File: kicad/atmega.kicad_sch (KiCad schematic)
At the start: 31 parts, among them J1 Conn_01x04_Pin, J3 Conn_02x03_Odd_Even, J4 Conn_01x03_Pin, J5 Conn_01x06_Pin, J6 Conn_01x04_Pin, SW1 SW_Push, U1 ATmega164P-20P, Y1 18.341MHz

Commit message: minor schematic updayes
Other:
- note added: "Note: can use internal PAx pull-ups (possibly) Maybe change to 680R to use similar resistors to the LEDs"
- note removed: "Note: can use internal PAx pull-ups (possibly)"
- moved on the sheet: R18, R9
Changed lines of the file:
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@@
 		)
 	)
-	(text "Note: can use internal PAx pull-ups (possibly)\n"
+	(text "Note: can use internal PAx pull-ups (possibly)\nMaybe change to 680R to use similar resistors to the LEDs"
 		(exclude_from_sim no)
-		(at 179.832 18.796 0)
+		(at 155.956 29.718 0)
 		(effects
 			(font
 				(size 1.27 1.27)
 			)
+			(justify left)
 		)
 	)
@@
 	(wire
 		(pts
-			(xy 189.23 81.28) (xy 189.23 77.47)
+			(xy 207.01 72.39) (xy 207.01 68.58)
 		)
 		(stroke
@@
 	(wire
 		(pts
-			(xy 193.04 81.28) (xy 189.23 81.28)
+			(xy 210.82 72.39) (xy 207.01 72.39)
 		)
 		(stroke
@@
 	(wire
 		(pts
-			(xy 193.04 85.09) (xy 180.34 85.09)
+			(xy 210.82 76.2) (xy 198.12 76.2)
 		)
 		(stroke
@@
 	(wire
 		(pts
-			(xy 180.34 85.09) (xy 180.34 77.47)
+			(xy 198.12 76.2) (xy 198.12 68.58)
 		)
 		(stroke
@@
 	(hierarchical_label "SCL"
 		(shape bidirectional)
-		(at 193.04 81.28 0)
+		(at 210.82 72.39 0)
 		(effects
 			(font
@@
 	(hierarchical_label "SDA"
 		(shape bidirectional)
-		(at 193.04 85.09 0)
+		(at 210.82 76.2 0)
 		(effects
 			(font
@@
 	(symbol
 		(lib_id "Device:R")
-		(at 189.23 73.66 0)
+		(at 207.01 64.77 0)
 		(unit 1)
 		(exclude_from_sim no)
@@
 		(fields_autoplaced yes)
 		(property "Reference" "R18"
-			(at 191.77 72.3899 0)
+			(at 209.55 63.4999 0)
 			(effects
 				(font
@@
 		)
 		(property "Value" "4K7"
-			(at 191.77 74.9299 0)
+			(at 209.55 66.0399 0)
 			(effects
 				(font
@@
 		)
 		(property "Footprint" "Resistor_THT:R_Axial_DIN0207_L6.3mm_D2.5mm_P10.16mm_Horizontal"
-			(at 187.452 73.66 90)
+			(at 205.232 64.77 90)
 			(effects
 				(font
@@
 		)
 		(property "Datasheet" "~"
-			(at 189.23 73.66 0)
+			(at 207.01 64.77 0)
 			(effects
 				(font
@@
 		)
 		(property "Description" "Resistor"
-			(at 189.23 73.66 0)
+			(at 207.01 64.77 0)
 			(effects
 				(font
@@
 	(symbol
 		(lib_id "power:VCC")
-		(at 189.23 69.85 0)
+		(at 207.01 60.96 0)
 		(unit 1)
 		(exclude_from_sim no)
@@
 		(fields_autoplaced yes)
 		(property "Reference" "#PWR040"
-			(at 189.23 73.66 0)
+			(at 207.01 64.77 0)
 			(effects
 				(font
@@
 		)
 		(property "Value" "VCC"
-			(at 189.23 64.77 0)
+			(at 207.01 55.88 0)
 			(effects
 				(font
@@
 		)
 		(property "Footprint" ""
-			(at 189.23 69.85 0)
+			(at 207.01 60.96 0)
 			(effects
 				(font
@@
 		)
 		(property "Datasheet" ""
-			(at 189.23 69.85 0)
+			(at 207.01 60.96 0)
 			(effects
 				(font
@@
 		)
 		(property "Description" "Power symbol creates a global label with name \"VCC\""
-			(at 189.23 69.85 0)
+			(at 207.01 60.96 0)
 			(effects
 				(font
@@
 	(symbol
 		(lib_id "power:VCC")
-		(at 180.34 69.85 0)
+		(at 198.12 60.96 0)
 		(unit 1)
 		(exclude_from_sim no)
@@
 		(fields_autoplaced yes)
 		(property "Reference" "#PWR041"
-			(at 180.34 73.66 0)
+			(at 198.12 64.77 0)
 			(effects
 				(font
@@
 		)
 		(property "Value" "VCC"
-			(at 180.34 64.77 0)
+			(at 198.12 55.88 0)
 			(effects
 				(font
@@
 		)
 		(property "Footprint" ""
-			(at 180.34 69.85 0)
+			(at 198.12 60.96 0)
 			(effects
 				(font
@@
 		)
 		(property "Datasheet" ""
-			(at 180.34 69.85 0)
+			(at 198.12 60.96 0)
 			(effects
 				(font
@@
 		)
 		(property "Description" "Power symbol creates a global label with name \"VCC\""
-			(at 180.34 69.85 0)
+			(at 198.12 60.96 0)
 			(effects
 				(font
@@
 	(symbol
 		(lib_id "Device:R")
-		(at 180.34 73.66 0)
+		(at 198.12 64.77 0)
 		(unit 1)
 		(exclude_from_sim no)
@@
 		(fields_autoplaced yes)
 		(property "Reference" "R9"
-			(at 182.88 72.3899 0)
+			(at 200.66 63.4999 0)
 			(effects
 				(font
@@
 		)
 		(property "Value" "4K7"
-			(at 182.88 74.9299 0)
+			(at 200.66 66.0399 0)
 			(effects
 				(font
@@
 		)
 		(property "Footprint" "Resistor_THT:R_Axial_DIN0207_L6.3mm_D2.5mm_P10.16mm_Horizontal"
-			(at 178.562 73.66 90)
+			(at 196.342 64.77 90)
 			(effects
 				(font
@@
 		)
 		(property "Datasheet" "~"
-			(at 180.34 73.66 0)
+			(at 198.12 64.77 0)
 			(effects
 				(font
@@
 		)
 		(property "Description" "Resistor"
-			(at 180.34 73.66 0)
+			(at 198.12 64.77 0)
 			(effects
 				(font

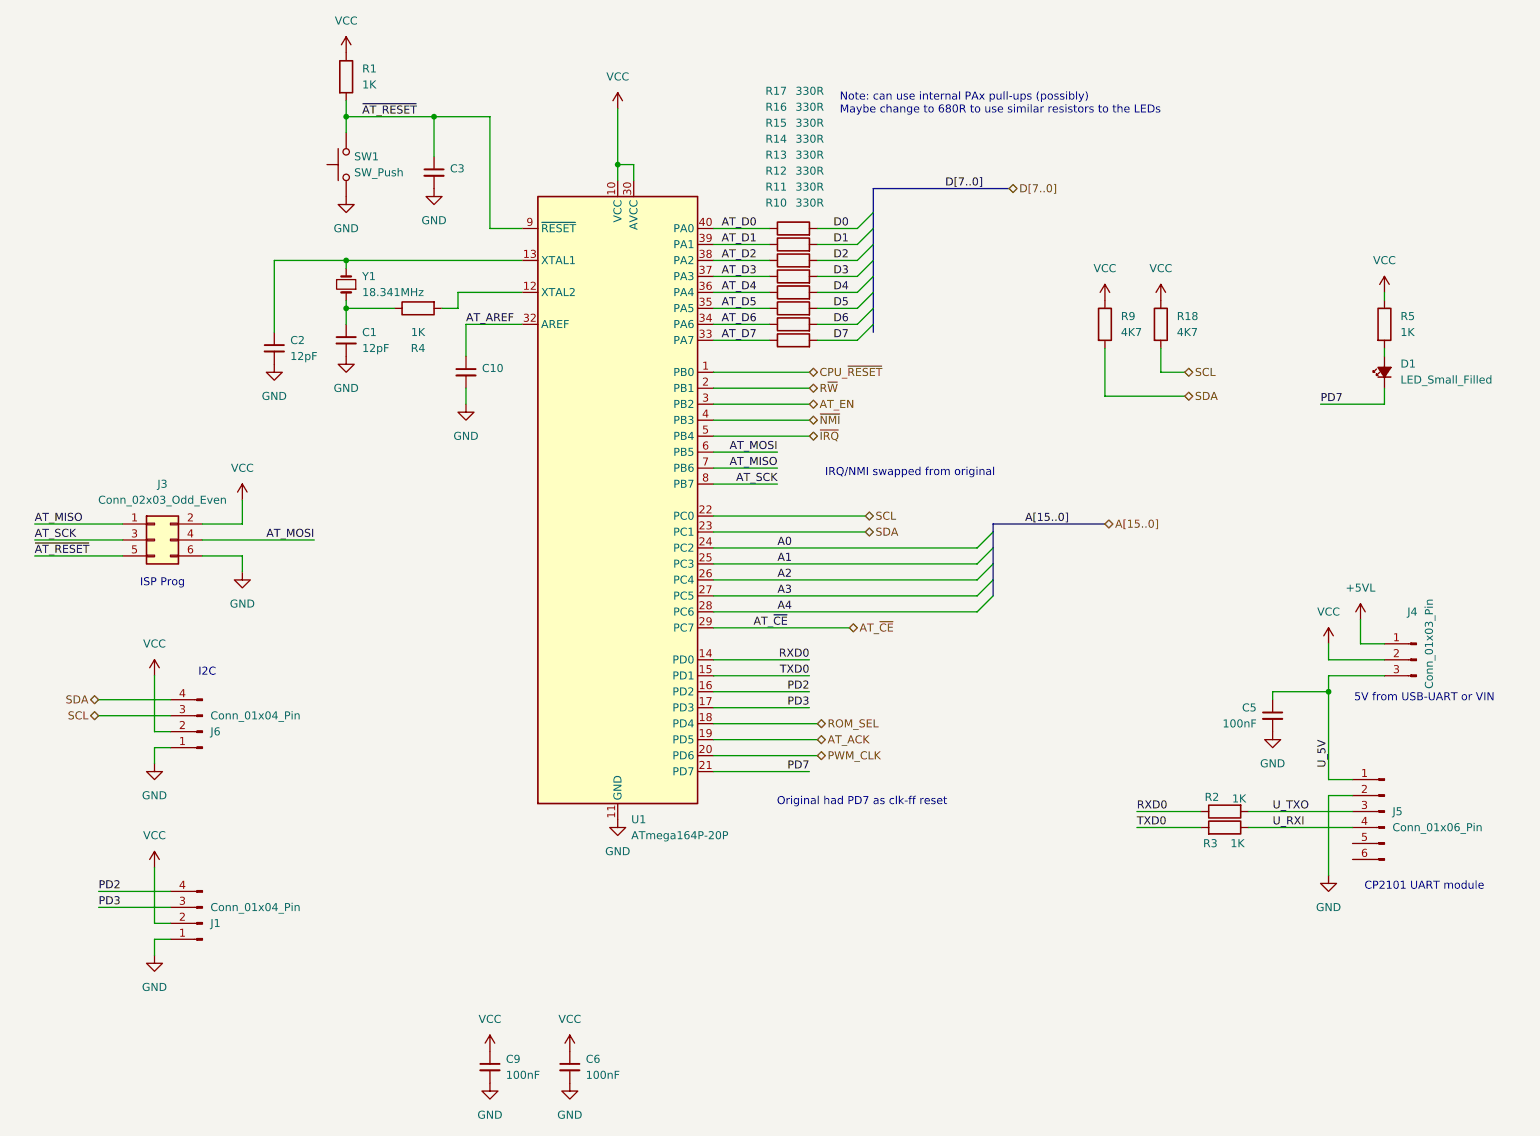
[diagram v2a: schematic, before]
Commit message: value updates, fix ROM ~WE
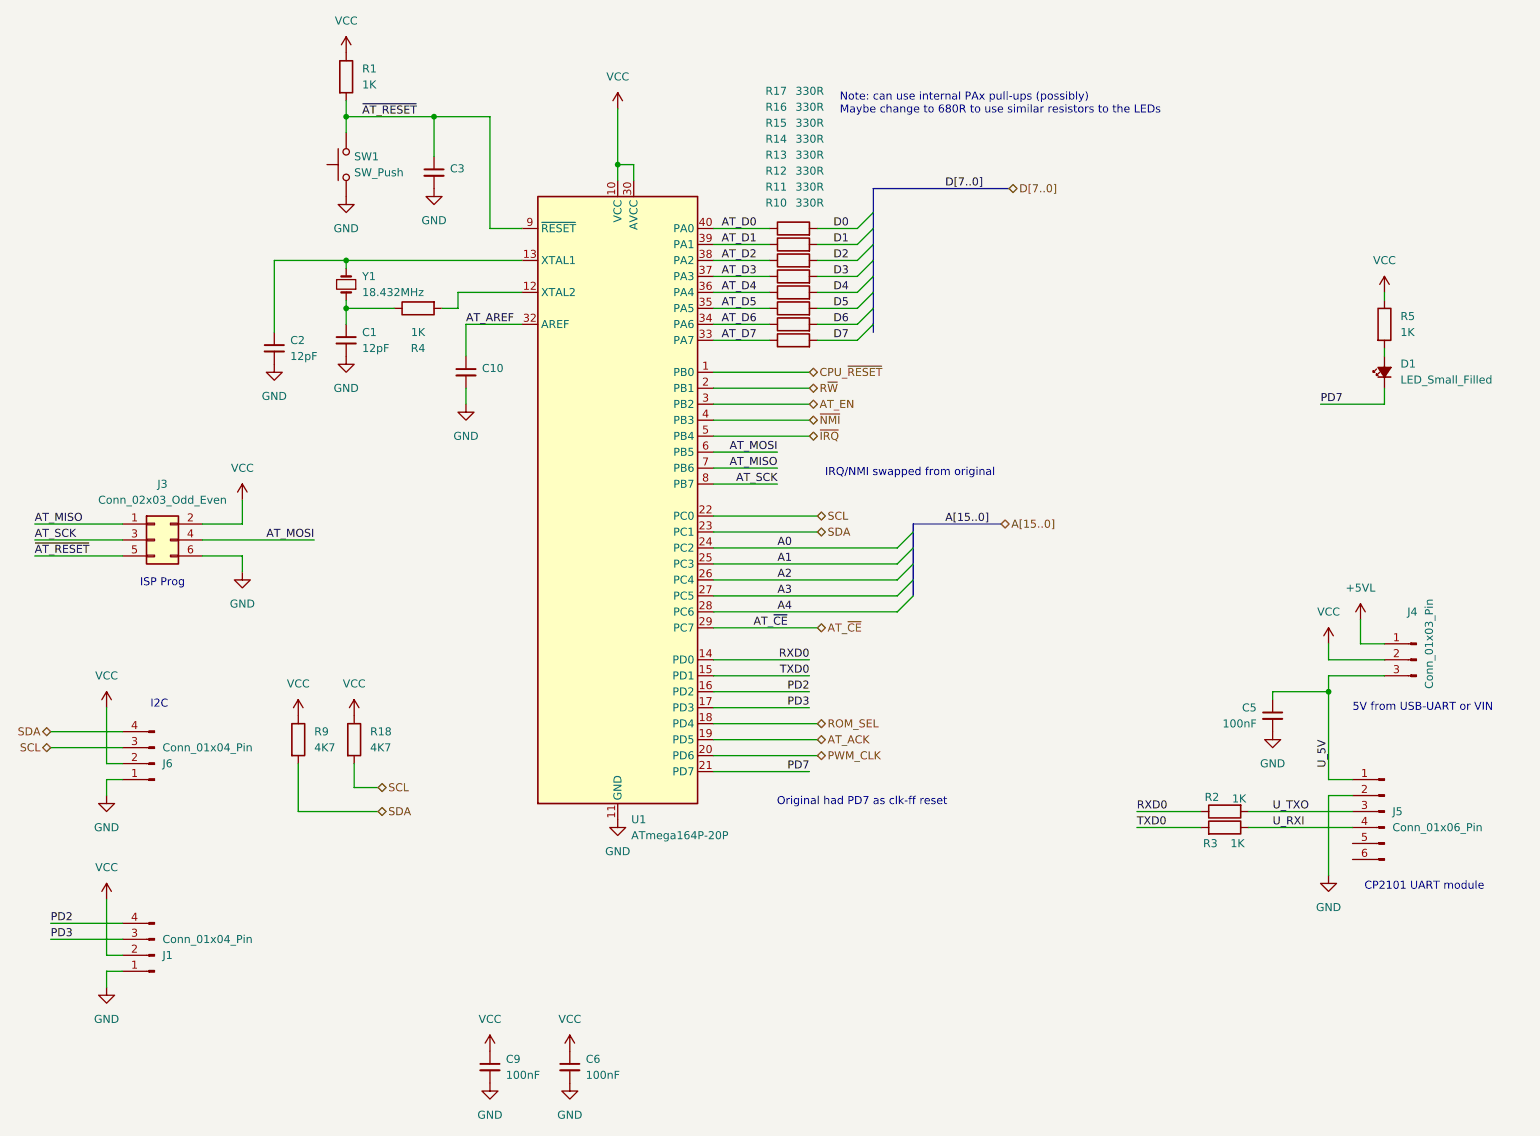
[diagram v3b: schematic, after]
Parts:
- Y1: value 18.341MHz -> 18.432MHz
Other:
- moved on the sheet: J1, J6, R18, R9

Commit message: pcb updates, remove resistor on xtal, smaller board
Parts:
- removed R4: 1K, Resistor_THT:R_Axial_DIN0207_L6.3mm_D2.5mm_P10.16mm_Horizontal, symbol Device:R
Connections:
- net AT_XTO: now reaches C1.1, Y1.1
- net AT_XTO: now also U1.12 (XTAL2)
- net AT_XTI: now reaches C2.1, U1.13 (XTAL1), Y1.2
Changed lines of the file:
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@@
 	(wire
 		(pts
-			(xy 92.71 62.23) (xy 95.25 62.23)
-		)
-		(stroke
-			(width 0)
-			(type default)
-		)
-	)
-	(wire
-		(pts
 			(xy 135.89 87.63) (xy 146.05 87.63)
 		)
@@
 	(wire
 		(pts
-			(xy 77.47 62.23) (xy 85.09 62.23)
+			(xy 77.47 62.23) (xy 95.25 62.23)
 		)
 		(stroke
@@
 		)
 	)
+	(label "AT_XTI"
+		(at 96.52 54.61 0)
+		(effects
+			(font
+				(size 1.27 1.27)
+			)
+			(justify left bottom)
+		)
+	)
 	(label "D4"
 		(at 154.94 59.69 0)
@@
 		)
 	)
+	(label "AT_XTO"
+		(at 96.52 59.69 0)
+		(effects
+			(font
+				(size 1.27 1.27)
+			)
+			(justify left bottom)
+		)
+	)
 	(label "AT_MISO"
 		(at 27.94 96.52 0)
@@
 					(unit 1)
 				)
-			)
-		)
-	)
-	(symbol
-		(lib_id "Device:R")
-		(at 88.9 62.23 90)
-		(mirror x)
-		(unit 1)
-		(exclude_from_sim no)
-		(in_bom yes)
-		(on_board yes)
-		(dnp no)
-		(property "Reference" "R4"
-			(at 88.9 68.58 90)
-			(effects
-				(font
-					(size 1.27 1.27)
-				)
-			)
-		)
-		(property "Value" "1K"
-			(at 88.9 66.04 90)
-			(effects
-				(font
-					(size 1.27 1.27)
-				)
-			)
-		)
-		(property "Footprint" "Resistor_THT:R_Axial_DIN0207_L6.3mm_D2.5mm_P10.16mm_Horizontal"
-			(at 88.9 60.452 90)
-			(effects
-				(font
-					(size 1.27 1.27)
-				)
-				(hide yes)
-			)
-		)
-		(property "Datasheet" "~"
-			(at 88.9 62.23 0)
-			(effects
-				(font
-					(size 1.27 1.27)
-				)
-				(hide yes)
-			)
-		)
-		(property "Description" "Resistor"
-			(at 88.9 62.23 0)
-			(effects
-				(font
-					(size 1.27 1.27)
-				)
-				(hide yes)
-			)
-		)
-		(pin "2"
-		)
-		(pin "1"
-		)
-		(instances
-			(project "6502atty"
-				(path "/f612fa92-d5fa-4cb5-a666-c1c24e7cbb30/83b01514-6b56-4f3e-9a42-17260f217a5e"
-					(reference "R4")
-					(unit 1)
-				)

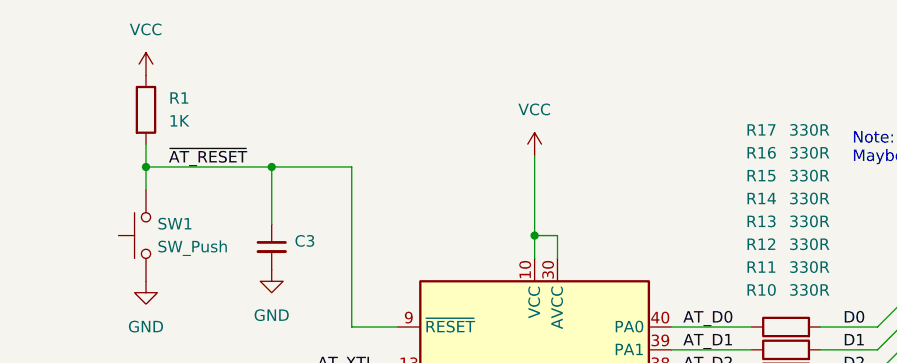
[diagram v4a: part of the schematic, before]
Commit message: add note on AVR nRESET
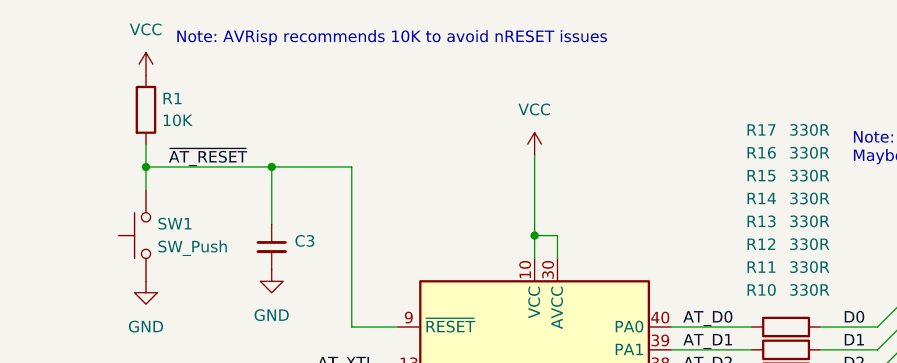
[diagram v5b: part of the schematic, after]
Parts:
- R1: value 1K -> 10K
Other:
- note added: "Note: AVRisp recommends 10K to avoid nRESET issues"
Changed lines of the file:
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@@
 		)
 	)
+	(text "Note: AVRisp recommends 10K to avoid nRESET issues"
+		(exclude_from_sim no)
+		(at 80.772 17.526 0)
+		(effects
+			(font
+				(size 1.27 1.27)
+			)
+			(justify left)
+		)
+	)
 	(junction
 		(at 120.65 39.37)
@@
 		(fields_autoplaced yes)
 		(property "Reference" "R1"
-			(at 80.01 24.1299 0)
+			(at 79.248 24.1878 0)
 			(effects
 				(font
@@
 			)
 		)
-		(property "Value" "1K"
-			(at 80.01 26.6699 0)
+		(property "Value" "10K"
+			(at 79.248 26.6121 0)
 			(effects
 				(font

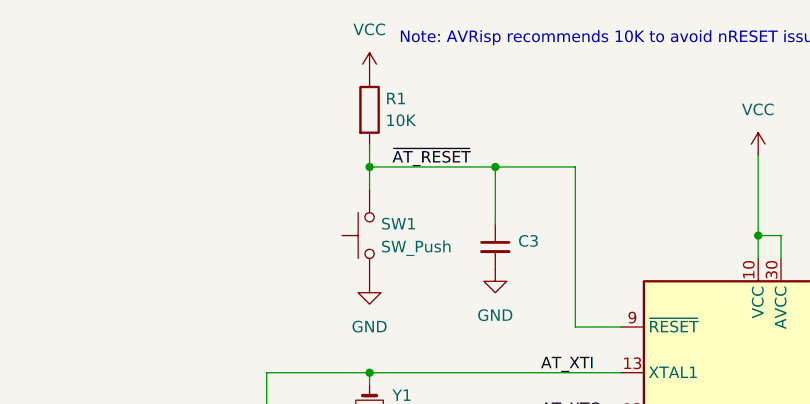
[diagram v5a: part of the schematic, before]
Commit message: pcb: add option for radial instead of axial capacitors
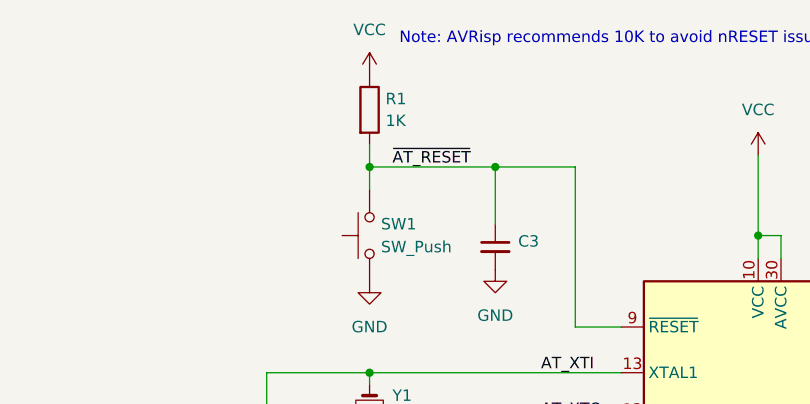
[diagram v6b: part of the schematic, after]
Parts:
- R1: value 10K -> 1K; footprint Resistor_THT:R_Axial_DIN0207_L6.3mm_D2.5mm_P10.16mm_Horizontal -> Resistor_THT:R_Axial_DIN0207_L6.3mm_D2.5mm_P2.54mm_Vertical
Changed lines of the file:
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@@
 			)
 		)
-		(property "Value" "10K"
+		(property "Value" "1K"
 			(at 79.248 26.6121 0)
 			(effects
@@
 			)
 		)
-		(property "Footprint" "Resistor_THT:R_Axial_DIN0207_L6.3mm_D2.5mm_P10.16mm_Horizontal"
+		(property "Footprint" "Resistor_THT:R_Axial_DIN0207_L6.3mm_D2.5mm_P2.54mm_Vertical"
 			(at 75.692 25.4 90)
 			(effects
@@
 			)
 		)
-		(property "Description" "Resistor"
+		(property "Description" ""
 			(at 77.47 25.4 0)
 			(effects

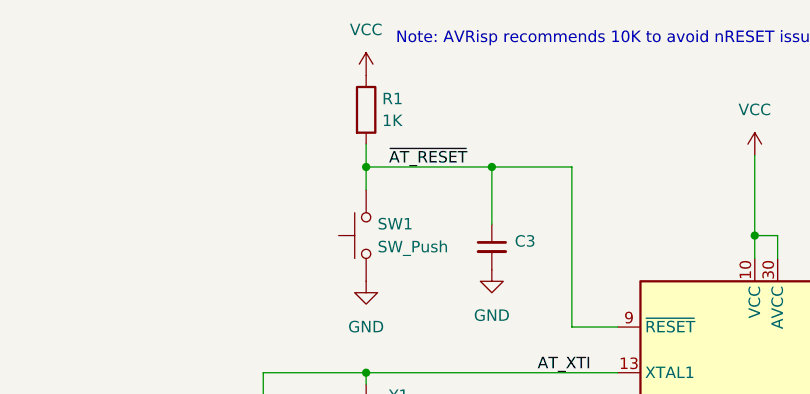
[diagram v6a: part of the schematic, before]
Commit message: pcb: route tidying, reduce size, re-do teardrops
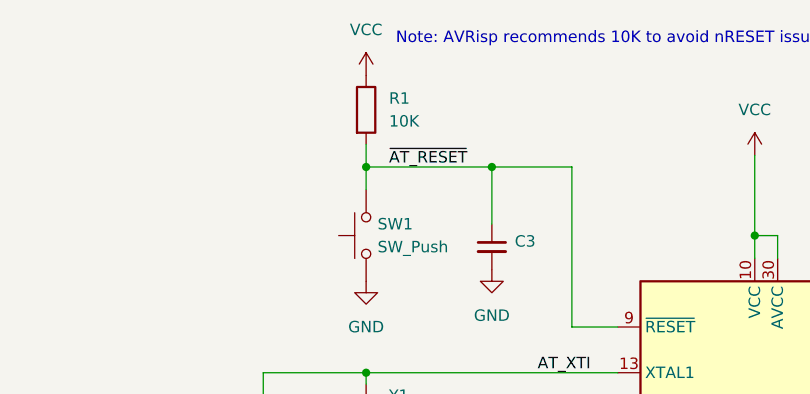
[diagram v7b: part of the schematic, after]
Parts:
- R1: value 1K -> 10K
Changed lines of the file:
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@@
 		(fields_autoplaced yes)
 		(property "Reference" "R1"
-			(at 79.248 24.1878 0)
+			(at 80.01 24.1299 0)
 			(effects
 				(font
@@
 			)
 		)
-		(property "Value" "1K"
-			(at 79.248 26.6121 0)
+		(property "Value" "10K"
+			(at 80.01 26.6699 0)
 			(effects
 				(font
